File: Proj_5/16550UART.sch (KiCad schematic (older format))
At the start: 2 parts, among them U14 16550

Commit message: Dont be wonky:
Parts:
- gave numbers to parts that had none: 1
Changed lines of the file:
@@
 P 5600 1350
 AR Path="/5EA98353/5EA6B70D" Ref="C?"  Part="1"
-AR Path="/5EA98A67/5EA6B70D" Ref="C?"  Part="1"
-F 0 "C?" V 5348 1350 50  0000 C CNN
+AR Path="/5EA98A67/5EA6B70D" Ref="C10"  Part="1"
+F 0 "C10" V 5348 1350 50  0000 C CNN
 F 1 "0.1uF" V 5439 1350 50  0000 C CNN
 F 2 "" H 5638 1200 50  0001 C CNN

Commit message: Rerouted Ext Wires, UART Mostly Complete, All Headers Added
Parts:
- added C?: 0.1uF, symbol Device:C
- added J?: DSUB-9, DSUB-9, symbol DSUB-9:DSUB-9
- added U?: max235cpg, max235cpg, symbol max235cpg:max235cpg
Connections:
- net GND: now reaches C10.1
- net GND: now also U14.20 (GND), U14.25 (~ADS~), C?.2, J?.5 (GND), U?.11 (GND)
- net at C10.2: now also U14.40 (VCC)
- net D0: now reaches U14.1 (D0)
- net at U14.10 (SIN): now also U?.23 (R3OUT)
- net at U14.11 (SOUT): now also U?.8 (T1IN)
- net ~WR: now reaches U14.18 (~WR~)
- net D1: now reaches U14.2 (D1)
- net ~RD: now reaches U14.21 (~RD~)
- net D2: now reaches U14.3 (D2)
- net IR3: now reaches U14.30 (INTR)
- net at U14.32 (~RTS~): now also J?.7 (RTS)
- net at U14.33 (~DTR~): now also J?.4 (DTR)
- net RESET: now reaches U14.35 (MR)
- net at U14.36 (~CTS~): now also J?.8 (CTS)
- net at U14.37 (~DSR~): now also J?.6 (DSR)
- net at U14.38 (~DCD~): now also J?.1 (DCD)
- net D3: now reaches U14.4 (D3)
- net D4: now reaches U14.5 (D4)
- net D5: now reaches U14.6 (D5)
- net D6: now reaches U14.7 (D6)
- net D7: now reaches U14.8 (D7)
- net MAIN_CLOCK: now reaches U14.9 (RCLK)
- new net: J?.2 (RDX), U?.24 (R3IN)
- new net: J?.3 (TDX), U?.3 (T1OUT)
- new net +5V: C?.1, U?.12 (VCC)
- no-connect marks 0 -> 28
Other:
- note added: "235 Needs Enables But from where"
- moved on the sheet: C10, U14

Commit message: Monch
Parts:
- added R?: 1K, symbol Device:R
- added U?: PAL16L8, symbol Logic_Programmable:PAL16L8
- added U? (x2): 74AHC1G02, symbol 74xGxx:74AHC1G02
- added U?: 74LVC1G08, symbol 74xGxx:74LVC1G08
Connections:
- net GND: now also U?.21 (SHDN), U?.3 (GND), U?.3 (GND), U?.3 (GND)
- net VCC: now reaches U?.20 (*EN)
- net VCC: now also R?.2, U?.5 (VCC), U?.5 (VCC), U?.5 (VCC)
- net at U14.12 (CS0): now also U14.13 (CS1), R?.1
- net at U14.14 (~CS2~): now also U?.12 (IO8)
- net A3: now reaches U14.26 (A2)
- net A2: now reaches U14.27 (A1)
- net A1: now reaches U14.28 (A0)
- new net: U?.16 (IO4), U?.4
- new net: U?.2, U?.4
- new net: U?.1, U?.4
- new net A0: U?.1 (I1)
- new net A10: U?.8 (I8)
- new net A11: U?.9 (I9)
- new net A12: U?.11 (I10)
- new net A13: U?.13 (IO7)
- new net A14: U?.14 (IO6)
- new net A15: U?.15 (IO5)
- new net A16: U?.2
- new net A17: U?.1
- new net A18: U?.2
- new net A19: U?.1
- new net A4: U?.2 (I2)
- new net A5: U?.3 (I3)
- new net A6: U?.4 (I4)
- new net A7: U?.5 (I5)
- new net A8: U?.6 (I6)
- new net A9: U?.7 (I7)
- no-connect marks 28 -> 31
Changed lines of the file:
@@
 NoConn ~ 8200 7800
 NoConn ~ 8200 8100
+Text HLabel 8200 7100 0    50   Input ~ 0
+A1
+Text HLabel 8200 7200 0    50   Input ~ 0
+A2
+$Comp
+L Logic_Programmable:PAL16L8 U?
+U 1 1 5EA83B43
+P 5400 7250
+F 0 "U?" H 5400 8131 50  0000 C CNN
+F 1 "PAL16L8" H 5400 8040 50  0000 C CNN
+F 2 "" H 5400 7250 50  0001 C CNN
+F 3 "" H 5400 7250 50  0001 C CNN
+	1    5400 7250
+	1    0    0    -1
+$EndComp
+Text HLabel 8200 7300 0    50   Input ~ 0
+A3
+Text HLabel 4900 6850 0    50   Input ~ 0
+A4
+Text HLabel 4900 6950 0    50   Input ~ 0
+A5
+Text HLabel 4900 7050 0    50   Input ~ 0
+A6
+Text HLabel 4900 7150 0    50   Input ~ 0
+A7
+Text HLabel 4900 7250 0    50   Input ~ 0
+A8
+Text HLabel 4900 7350 0    50   Input ~ 0
+A9
+Text HLabel 4900 7450 0    50   Input ~ 0
+A10
+Text HLabel 4900 7550 0    50   Input ~ 0
+A11
+Text HLabel 4900 7650 0    50   Input ~ 0
+A12
+Text HLabel 5900 7350 2    50   Input ~ 0
+A13
+Text HLabel 5900 7250 2    50   Input ~ 0
+A14
+Text HLabel 5900 7150 2    50   Input ~ 0
+A15
+Text HLabel 4900 6750 0    50   Input ~ 0
+A0
+$Comp
+L 74xGxx:74AHC1G02 U?
+U 1 1 5EA8FF70
+P 6250 5750
+F 0 "U?" V 6179 5880 50  0000 L CNN
+F 1 "74AHC1G02" V 6270 5880 50  0000 L CNN
+F 2 "" H 6250 5750 50  0001 C CNN
+F 3 "http://www.ti.com/lit/sg/scyt129e/scyt129e.pdf" H 6250 5750 50  0001 C CNN
+	1    6250 5750
+	0    1    1    0
+$EndComp
+$Comp
+L 74xGxx:74AHC1G02 U?
+U 1 1 5EA96A09
+P 6950 5750
+F 0 "U?" V 6879 5880 50  0000 L CNN
+F 1 "74AHC1G02" V 6970 5880 50  0000 L CNN
+F 2 "" H 6950 5750 50  0001 C CNN
+F 3 "http://www.ti.com/lit/sg/scyt129e/scyt129e.pdf" H 6950 5750 50  0001 C CNN
+	1    6950 5750
+	0    1    1    0
+$EndComp
+$Comp
+L 74xGxx:74LVC1G08 U?
+U 1 1 5EA99D66
+P 6600 6300
+F 0 "U?" V 6529 6430 50  0000 L CNN
+F 1 "74LVC1G08" V 6620 6430 50  0000 L CNN
+F 2 "" H 6600 6300 50  0001 C CNN
+F 3 "http://www.ti.com/lit/sg/scyt129e/scyt129e.pdf" H 6600 6300 50  0001 C CNN
+	1    6600 6300
+	0    1    1    0
+$EndComp
+Wire Wire Line
+	6650 6000 6950 6000
+Wire Wire Line
+	6550 6000 6250 6000
+Wire Wire Line
+	6600 6550 6600 7050
+Wire Wire Line
+	6600 7050 5900 7050
+Text HLabel 6200 5450 1    50   Input ~ 0
+A16
+Text HLabel 6300 5450 1    50   Input ~ 0
+A17
+Text HLabel 6900 5450 1    50   Input ~ 0
+A18
+Text HLabel 7000 5450 1    50   Input ~ 0
+A19
+Wire Wire Line
+	8200 7600 5900 7600
+Wire Wire Line
+	5900 7600 5900 7450
+$Comp
+L power:VCC #PWR?
+U 1 1 5EAA2831
+P 7400 7400
+F 0 "#PWR?" H 7400 7250 50  0001 C CNN
+F 1 "VCC" H 7417 7573 50  0000 C CNN
+F 2 "" H 7400 7400 50  0001 C CNN
+F 3 "" H 7400 7400 50  0001 C CNN
+	1    7400 7400
+	1    0    0    -1
+$EndComp
+Wire Wire Line
+	8200 7400 7950 7400
+Wire Wire Line
+	8200 7500 7950 7500
+Wire Wire Line
+	7950 7500 7950 7400
+$Comp
+L Device:R R?
+U 1 1 5EAA6766
+P 7550 7400
+F 0 "R?" V 7343 7400 50  0000 C CNN
+F 1 "1K" V 7434 7400 50  0000 C CNN
+F 2 "" V 7480 7400 50  0001 C CNN
+F 3 "~" H 7550 7400 50  0001 C CNN
+	1    7550 7400
+	0    1    1    0
+$EndComp
+Wire Wire Line
+	7700 7400 7950 7400
+Connection ~ 7950 7400
+NoConn ~ 5900 6750
+NoConn ~ 5900 6850
+NoConn ~ 5900 6950
+$Comp
+L power:GND #PWR?
+U 1 1 5EAB604F
+P 16650 7000
+F 0 "#PWR?" H 16650 6750 50  0001 C CNN
+F 1 "GND" V 16655 6872 50  0000 R CNN
+F 2 "" H 16650 7000 50  0001 C CNN
+F 3 "" H 16650 7000 50  0001 C CNN
+	1    16650 7000
+	0    -1   -1   0
+$EndComp
+$Comp
+L power:VCC #PWR?
+U 1 1 5EAB6B80
+P 14050 7000
+F 0 "#PWR?" H 14050 6850 50  0001 C CNN
+F 1 "VCC" H 14067 7173 50  0000 C CNN
+F 2 "" H 14050 7000 50  0001 C CNN
+F 3 "" H 14050 7000 50  0001 C CNN
+	1    14050 7000
+	1    0    0    -1
+$EndComp
 $EndSCHEMATC

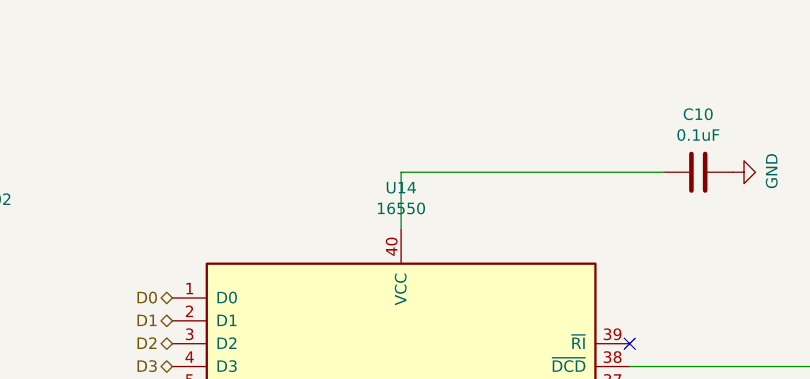
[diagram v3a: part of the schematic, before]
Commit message: Remaining LED Components Added, Final pins added to headers.
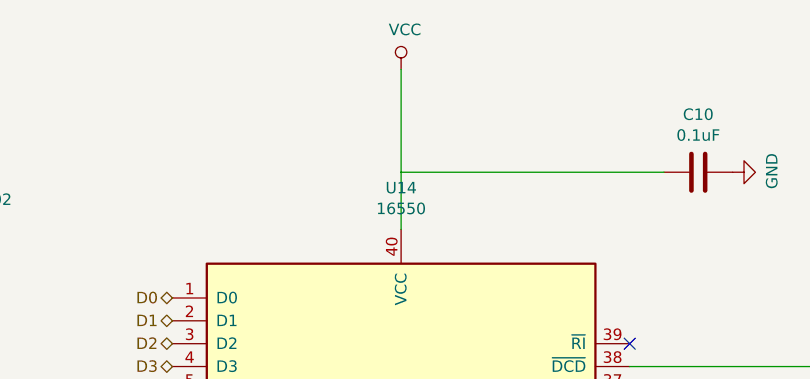
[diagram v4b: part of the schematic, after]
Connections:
- net VCC: now also C10.2, U14.40 (VCC)
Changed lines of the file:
@@
+	1    0    0    -1
+$EndComp
+Wire Wire Line
+	9200 5200 9200 5650
+$Comp
+L power:VCC #PWR?
+U 1 1 5F0AFF2A
+P 9200 5200
+F 0 "#PWR?" H 9200 5050 50  0001 C CNN
+F 1 "VCC" H 9217 5373 50  0000 C CNN
+F 2 "" H 9200 5200 50  0001 C CNN
+F 3 "" H 9200 5200 50  0001 C CNN
+	1    9200 5200
 	1    0    0    -1
 $EndComp

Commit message: Added Power Flags, finished no connects.
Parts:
- gave numbers to parts that had none: 8
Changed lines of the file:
@@
 $Descr A2 23386 16535
 encoding utf-8
-Sheet 9 9
+Sheet 9 10
 Title ""
 Date ""
@@
 P 19000 7100
 AR Path="/5EAF7226/5EA3C31E" Ref="J?"  Part="1"
-AR Path="/5EA98A67/5EA3C31E" Ref="J?"  Part="1"
-F 0 "J?" H 19828 6753 60  0000 L CNN
+AR Path="/5EA98A67/5EA3C31E" Ref="J7"  Part="1"
+F 0 "J7" H 19828 6753 60  0000 L CNN
 F 1 "DSUB-9" H 19828 6647 60  0000 L CNN
 F 2 "DSUB-9" H 19600 6740 60  0001 C CNN
@@
 P 14050 7000
 AR Path="/5EAF7226/5EA3C324" Ref="U?"  Part="1"
-AR Path="/5EA98A67/5EA3C324" Ref="U?"  Part="1"
-F 0 "U?" H 15350 7387 60  0000 C CNN
+AR Path="/5EA98A67/5EA3C324" Ref="U55"  Part="1"
+F 0 "U55" H 15350 7387 60  0000 C CNN
 F 1 "max235cpg" H 15350 7281 60  0000 C CNN
 F 2 "max235cpg" H 15350 7240 60  0001 C CNN
@@
 P 15000 8600
 AR Path="/5EAF7226/5EA40B25" Ref="#PWR?"  Part="1"
-AR Path="/5EA98A67/5EA40B25" Ref="#PWR?"  Part="1"
-F 0 "#PWR?" H 15000 8350 50  0001 C CNN
+AR Path="/5EA98A67/5EA40B25" Ref="#PWR098"  Part="1"
+F 0 "#PWR098" H 15000 8350 50  0001 C CNN
 F 1 "GND" H 15005 8427 50  0000 C CNN
 F 2 "" H 15000 8600 50  0001 C CNN
@@
 P 9200 9300
 AR Path="/5EAF7226/5EA41175" Ref="#PWR?"  Part="1"
-AR Path="/5EA98A67/5EA41175" Ref="#PWR?"  Part="1"
-F 0 "#PWR?" H 9200 9050 50  0001 C CNN
+AR Path="/5EA98A67/5EA41175" Ref="#PWR095"  Part="1"
+F 0 "#PWR095" H 9200 9050 50  0001 C CNN
 F 1 "GND" H 9205 9127 50  0000 C CNN
 F 2 "" H 9200 9300 50  0001 C CNN
@@
 P 10650 5650
 AR Path="/5EAF7226/5EA41CE6" Ref="#PWR?"  Part="1"
-AR Path="/5EA98A67/5EA41CE6" Ref="#PWR?"  Part="1"
-F 0 "#PWR?" H 10650 5400 50  0001 C CNN
+AR Path="/5EA98A67/5EA41CE6" Ref="#PWR096"  Part="1"
+F 0 "#PWR096" H 10650 5400 50  0001 C CNN
 F 1 "GND" H 10655 5477 50  0000 C CNN
 F 2 "" H 10650 5650 50  0001 C CNN
@@
 NoConn ~ 8200 8600
 $Comp
-L power:+5V #PWR?
+L power:+5V #PWR099
 U 1 1 5EA81CD6
 P 15700 9250
-F 0 "#PWR?" H 15700 9100 50  0001 C CNN
+F 0 "#PWR099" H 15700 9100 50  0001 C CNN
 F 1 "+5V" V 15715 9378 50  0000 L CNN
 F 2 "" H 15700 9250 50  0001 C CNN
@@
 P 16100 8600
 AR Path="/5EAF7226/5EA3C332" Ref="#PWR?"  Part="1"
-AR Path="/5EA98A67/5EA3C332" Ref="#PWR?"  Part="1"
-F 0 "#PWR?" H 16100 8350 50  0001 C CNN
+AR Path="/5EA98A67/5EA3C332" Ref="#PWR0100"  Part="1"
+F 0 "#PWR0100" H 16100 8350 50  0001 C CNN
 F 1 "GND" H 16105 8427 50  0000 C CNN
 F 2 "" H 16100 8600 50  0001 C CNN
@@
 AR Path="/5EA98353/5EA3C32A" Ref="C?"  Part="1"
 AR Path="/5EAF7226/5EA3C32A" Ref="C?"  Part="1"
-AR Path="/5EA98A67/5EA3C32A" Ref="C?"  Part="1"
-F 0 "C?" V 15698 8600 50  0000 C CNN
+AR Path="/5EA98A67/5EA3C32A" Ref="C20"  Part="1"
+F 0 "C20" V 15698 8600 50  0000 C CNN
 F 1 "0.1uF" V 15789 8600 50  0000 C CNN
 F 2 "" H 15988 8450 50  0001 C CNN
@@
 P 19550 8200
 AR Path="/5EAF7226/5EAA0E88" Ref="#PWR?"  Part="1"
-AR Path="/5EA98A67/5EAA0E88" Ref="#PWR?"  Part="1"
-F 0 "#PWR?" H 19550 7950 50  0001 C CNN
+AR Path="/5EA98A67/5EAA0E88" Ref="#PWR0106"  Part="1"
+F 0 "#PWR0106" H 19550 7950 50  0001 C CNN
 F 1 "GND" H 19555 8027 50  0000 C CNN
 F 2 "" H 19550 8200 50  0001 C CNN
@@
 P 7850 8800
 AR Path="/5EAF7226/5EAA4D1F" Ref="#PWR?"  Part="1"
-AR Path="/5EA98A67/5EAA4D1F" Ref="#PWR?"  Part="1"
-F 0 "#PWR?" H 7850 8550 50  0001 C CNN
+AR Path="/5EA98A67/5EAA4D1F" Ref="#PWR093"  Part="1"
+F 0 "#PWR093" H 7850 8550 50  0001 C CNN
 F 1 "GND" H 7855 8627 50  0000 C CNN
 F 2 "" H 7850 8800 50  0001 C CNN
@@
 A2
 $Comp
-L Logic_Programmable:PAL16L8 U?
+L Logic_Programmable:PAL16L8 U51
 U 1 1 5EA83B43
 P 5400 7250
-F 0 "U?" H 5400 8131 50  0000 C CNN
+F 0 "U51" H 5400 8131 50  0000 C CNN
 F 1 "PAL16L8" H 5400 8040 50  0000 C CNN
 F 2 "" H 5400 7250 50  0001 C CNN
@@
 A0
 $Comp
-L 74xGxx:74AHC1G02 U?
+L 74xGxx:74AHC1G02 U52
 U 1 1 5EA8FF70
 P 6250 5750
-F 0 "U?" V 6179 5880 50  0000 L CNN
+F 0 "U52" V 6179 5880 50  0000 L CNN
 F 1 "74AHC1G02" V 6270 5880 50  0000 L CNN
 F 2 "" H 6250 5750 50  0001 C CNN
@@
 $EndComp
 $Comp
-L 74xGxx:74AHC1G02 U?
+L 74xGxx:74AHC1G02 U54
 U 1 1 5EA96A09
 P 6950 5750
-F 0 "U?" V 6879 5880 50  0000 L CNN
+F 0 "U54" V 6879 5880 50  0000 L CNN
 F 1 "74AHC1G02" V 6970 5880 50  0000 L CNN
 F 2 "" H 6950 5750 50  0001 C CNN
@@
 $EndComp
 $Comp
-L 74xGxx:74LVC1G08 U?
+L 74xGxx:74LVC1G08 U53
 U 1 1 5EA99D66
 P 6600 6300
-F 0 "U?" V 6529 6430 50  0000 L CNN
+F 0 "U53" V 6529 6430 50  0000 L CNN
 F 1 "74LVC1G08" V 6620 6430 50  0000 L CNN
 F 2 "" H 6600 6300 50  0001 C CNN
@@
 	5900 7600 5900 7450
 $Comp
-L power:VCC #PWR?
+L power:VCC #PWR092
 U 1 1 5EAA2831
 P 7400 7400
-F 0 "#PWR?" H 7400 7250 50  0001 C CNN
+F 0 "#PWR092" H 7400 7250 50  0001 C CNN
 F 1 "VCC" H 7417 7573 50  0000 C CNN
 F 2 "" H 7400 7400 50  0001 C CNN
@@
 	7950 7500 7950 7400
 $Comp
-L Device:R R?
+L Device:R R18
 U 1 1 5EAA6766
 P 7550 7400
-F 0 "R?" V 7343 7400 50  0000 C CNN
+F 0 "R18" V 7343 7400 50  0000 C CNN
 F 1 "1K" V 7434 7400 50  0000 C CNN
 F 2 "" V 7480 7400 50  0001 C CNN
@@
 NoConn ~ 5900 6950
 $Comp
-L power:GND #PWR?
+L power:GND #PWR0105
 U 1 1 5EAB604F
 P 16650 7000
-F 0 "#PWR?" H 16650 6750 50  0001 C CNN
+F 0 "#PWR0105" H 16650 6750 50  0001 C CNN
 F 1 "GND" V 16655 6872 50  0000 R CNN
 F 2 "" H 16650 7000 50  0001 C CNN
@@
 $EndComp
 $Comp
-L power:VCC #PWR?
+L power:VCC #PWR097
 U 1 1 5EAB6B80
 P 14050 7000
-F 0 "#PWR?" H 14050 6850 50  0001 C CNN
+F 0 "#PWR097" H 14050 6850 50  0001 C CNN
 F 1 "VCC" H 14067 7173 50  0000 C CNN
 F 2 "" H 14050 7000 50  0001 C CNN
@@
 	9200 5200 9200 5650
 $Comp
-L power:VCC #PWR?
+L power:VCC #PWR094
 U 1 1 5F0AFF2A
 P 9200 5200
-F 0 "#PWR?" H 9200 5050 50  0001 C CNN
+F 0 "#PWR094" H 9200 5050 50  0001 C CNN
 F 1 "VCC" H 9217 5373 50  0000 C CNN
 F 2 "" H 9200 5200 50  0001 C CNN

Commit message: Finished Most of power flags, power connector header, added hierachical pins to a few sheets.
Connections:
- net +5V is gone; now on net VCC: C20.1, U55.12 (VCC)
- net GND: now also U51.10 (GND)
- net VCC: now also U51.20 (VCC)
- net D0 renamed D8
- net D1 renamed D9
- net D2 renamed D10
- net D3 renamed D11
- net D4 renamed D12
- net D5 renamed D13
- net D6 renamed D14
- net D7 renamed D15
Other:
- note removed: "235 Needs Enables But from where"
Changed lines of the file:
@@
 $Descr A2 23386 16535
 encoding utf-8
-Sheet 9 10
+Sheet 8 10
 Title ""
 Date ""
@@
 NoConn ~ 8200 8500
 NoConn ~ 8200 8600
-$Comp
-L power:+5V #PWR099
-U 1 1 5EA81CD6
-P 15700 9250
-F 0 "#PWR099" H 15700 9100 50  0001 C CNN
-F 1 "+5V" V 15715 9378 50  0000 L CNN
-F 2 "" H 15700 9250 50  0001 C CNN
-F 3 "" H 15700 9250 50  0001 C CNN
-	1    15700 9250
-	-1   0    0    1
-$EndComp
 Wire Wire Line
 	15700 8600 15600 8600
 Connection ~ 15700 8600
-Wire Wire Line
-	15700 8600 15700 9250
 $Comp
 L power:GND #PWR?
@@
 Text HLabel 8200 8700 0    50   Input ~ 0
 ~RD
-Text HLabel 8200 6900 0    50   BiDi ~ 0
-D7
-Text HLabel 8200 6800 0    50   BiDi ~ 0
-D6
-Text HLabel 8200 6700 0    50   BiDi ~ 0
-D5
-Text HLabel 8200 6600 0    50   BiDi ~ 0
-D4
-Text HLabel 8200 6500 0    50   BiDi ~ 0
-D3
-Text HLabel 8200 6400 0    50   BiDi ~ 0
-D2
-Text HLabel 8200 6300 0    50   BiDi ~ 0
-D1
-Text HLabel 8200 6200 0    50   BiDi ~ 0
-D0
 Wire Wire Line
 	8200 8800 7850 8800
@@
 NoConn ~ 10200 7300
 NoConn ~ 10200 7000
-Text Notes 13100 10400 0    118  ~ 0
-235 Needs Enables But from where
 NoConn ~ 8200 7800
 NoConn ~ 8200 8100
@@
 	1    0    0    -1
 $EndComp
+Text HLabel 8200 6200 0    50   BiDi ~ 0
+D8
+Text HLabel 8200 6300 0    50   BiDi ~ 0
+D9
+Text HLabel 8200 6400 0    50   BiDi ~ 0
+D10
+Text HLabel 8200 6500 0    50   BiDi ~ 0
+D11
+Text HLabel 8200 6600 0    50   BiDi ~ 0
+D12
+Text HLabel 8200 6700 0    50   BiDi ~ 0
+D13
+Text HLabel 8200 6800 0    50   BiDi ~ 0
+D14
+Text HLabel 8200 6900 0    50   BiDi ~ 0
+D15
+$Comp
+L power:PWR_FLAG #FLG?
+U 1 1 5EDA95FE
+P 7400 7400
+F 0 "#FLG?" H 7400 7475 50  0001 C CNN
+F 1 "PWR_FLAG" V 7400 7527 50  0000 L CNN
+F 2 "" H 7400 7400 50  0001 C CNN
+F 3 "~" H 7400 7400 50  0001 C CNN
+	1    7400 7400
+	0    -1   -1   0
+$EndComp
+Connection ~ 7400 7400
+Wire Wire Line
+	5400 6550 5200 6550
+Wire Wire Line
+	5200 6550 5200 6300
+Wire Wire Line
+	5400 7850 5400 8000
+$Comp
+L power:VCC #PWR?
+U 1 1 5EDADCA7
+P 5200 6300
+F 0 "#PWR?" H 5200 6150 50  0001 C CNN
+F 1 "VCC" H 5217 6473 50  0000 C CNN
+F 2 "" H 5200 6300 50  0001 C CNN
+F 3 "" H 5200 6300 50  0001 C CNN
+	1    5200 6300
+	1    0    0    -1
+$EndComp
+$Comp
+L power:GND #PWR?
+U 1 1 5EDB05EC
+P 5400 8000
+AR Path="/5EAF7226/5EDB05EC" Ref="#PWR?"  Part="1"
+AR Path="/5EA98A67/5EDB05EC" Ref="#PWR?"  Part="1"
+F 0 "#PWR?" H 5400 7750 50  0001 C CNN
+F 1 "GND" H 5405 7827 50  0000 C CNN
+F 2 "" H 5400 8000 50  0001 C CNN
+F 3 "" H 5400 8000 50  0001 C CNN
+	1    5400 8000
+	1    0    0    -1
+$EndComp
+$Comp
+L power:PWR_FLAG #FLG?
+U 1 1 5EDB2807
+P 5400 8000
+F 0 "#FLG?" H 5400 8075 50  0001 C CNN
+F 1 "PWR_FLAG" V 5400 8127 50  0000 L CNN
+F 2 "" H 5400 8000 50  0001 C CNN
+F 3 "~" H 5400 8000 50  0001 C CNN
+	1    5400 8000
+	0    -1   -1   0
+$EndComp
+$Comp
+L power:PWR_FLAG #FLG?
+U 1 1 5EDB3E22
+P 9200 5200
+F 0 "#FLG?" H 9200 5275 50  0001 C CNN
+F 1 "PWR_FLAG" V 9200 5327 50  0000 L CNN
+F 2 "" H 9200 5200 50  0001 C CNN
+F 3 "~" H 9200 5200 50  0001 C CNN
+	1    9200 5200
+	0    1    1    0
+$EndComp
+Connection ~ 9200 5200
+Connection ~ 5400 8000
+$Comp
+L power:PWR_FLAG #FLG?
+U 1 1 5EDB8A2E
+P 5200 6300
+F 0 "#FLG?" H 5200 6375 50  0001 C CNN
+F 1 "PWR_FLAG" V 5200 6427 50  0000 L CNN
+F 2 "" H 5200 6300 50  0001 C CNN
+F 3 "~" H 5200 6300 50  0001 C CNN
+	1    5200 6300
+	0    -1   -1   0
+$EndComp
+$Comp
+L power:PWR_FLAG #FLG?
+U 1 1 5EDBA7F8
+P 9200 9300
+F 0 "#FLG?" H 9200 9375 50  0001 C CNN
+F 1 "PWR_FLAG" V 9200 9427 50  0000 L CNN
+F 2 "" H 9200 9300 50  0001 C CNN
+F 3 "~" H 9200 9300 50  0001 C CNN
+	1    9200 9300
+	0    1    1    0
+$EndComp
+$Comp
+L power:VCC #PWR?
+U 1 1 5EDC0795
+P 15700 9600
+F 0 "#PWR?" H 15700 9450 50  0001 C CNN
+F 1 "VCC" H 15717 9773 50  0000 C CNN
+F 2 "" H 15700 9600 50  0001 C CNN
+F 3 "" H 15700 9600 50  0001 C CNN
+	1    15700 9600
+	-1   0    0    1
+$EndComp
+$Comp
+L power:PWR_FLAG #FLG?
+U 1 1 5EDC079B
+P 15700 9600
+F 0 "#FLG?" H 15700 9675 50  0001 C CNN
+F 1 "PWR_FLAG" V 15700 9727 50  0000 L CNN
+F 2 "" H 15700 9600 50  0001 C CNN
+F 3 "~" H 15700 9600 50  0001 C CNN
+	1    15700 9600
+	0    -1   -1   0
+$EndComp
+Connection ~ 15700 9600
+Wire Wire Line
+	15700 8600 15700 9600
+$Comp
+L power:PWR_FLAG #FLG?
+U 1 1 5EDC2E00
+P 19550 8200
+F 0 "#FLG?" H 19550 8275 50  0001 C CNN
+F 1 "PWR_FLAG" V 19550 8327 50  0000 L CNN
+F 2 "" H 19550 8200 50  0001 C CNN
+F 3 "~" H 19550 8200 50  0001 C CNN
+	1    19550 8200
+	0    -1   -1   0
+$EndComp
+$Comp
+L power:PWR_FLAG #FLG?
+U 1 1 5EDC65AB
+P 15000 8600
+F 0 "#FLG?" H 15000 8675 50  0001 C CNN
+F 1 "PWR_FLAG" V 15000 8727 50  0000 L CNN
+F 2 "" H 15000 8600 50  0001 C CNN
+F 3 "~" H 15000 8600 50  0001 C CNN
+	1    15000 8600
+	0    -1   -1   0
+$EndComp
+$Comp
+L power:PWR_FLAG #FLG?
+U 1 1 5EDC8FD2
+P 16650 7000
+F 0 "#FLG?" H 16650 7075 50  0001 C CNN
+F 1 "PWR_FLAG" V 16650 7127 50  0000 L CNN
+F 2 "" H 16650 7000 50  0001 C CNN
+F 3 "~" H 16650 7000 50  0001 C CNN
+	1    16650 7000
+	1    0    0    -1
+$EndComp
+$Comp
+L power:PWR_FLAG #FLG?
+U 1 1 5EDCA580
+P 14050 7000
+F 0 "#FLG?" H 14050 7075 50  0001 C CNN
+F 1 "PWR_FLAG" V 14050 7127 50  0000 L CNN
+F 2 "" H 14050 7000 50  0001 C CNN
+F 3 "~" H 14050 7000 50  0001 C CNN
+	1    14050 7000
+	0    -1   -1   0
+$EndComp
 $EndSCHEMATC
